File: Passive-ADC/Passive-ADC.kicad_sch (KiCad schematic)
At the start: 12 parts, among them J1 FPGA Terminal, J2 ADC Terminal

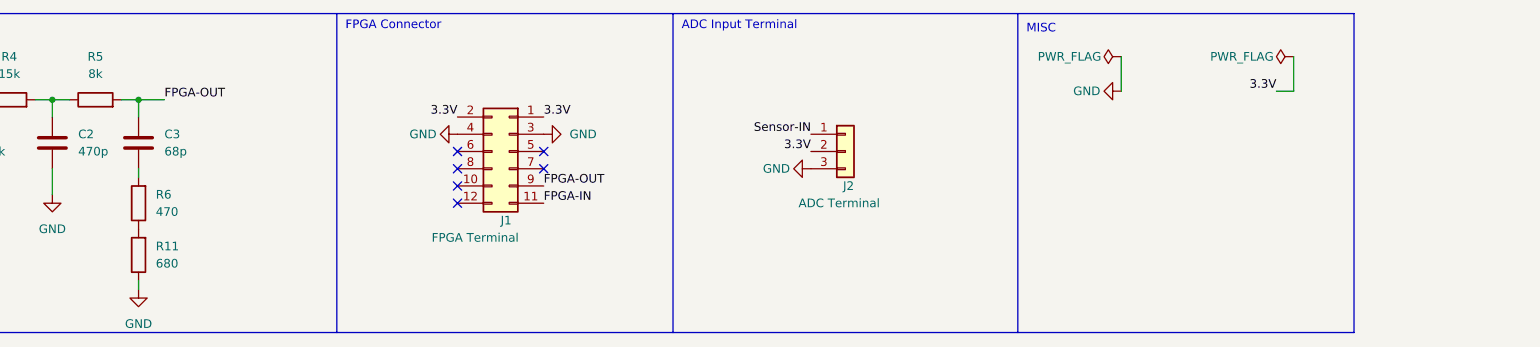
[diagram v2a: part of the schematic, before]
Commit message: Close to final pcb adjusted footprints and layout design incorperating voltage divider
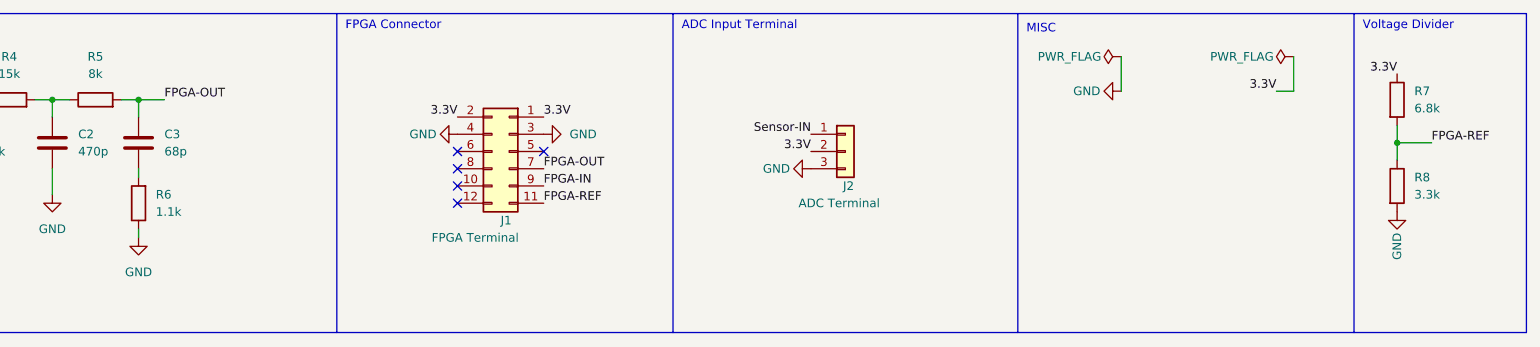
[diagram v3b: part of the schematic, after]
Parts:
- removed R11: 680, Resistor_SMD:R_0805_2012Metric_Pad1.20x1.40mm_HandSolder, symbol Device:R
- added R7: 6.8k, Resistor_SMD:R_0805_2012Metric_Pad1.20x1.40mm_HandSolder, symbol Device:R
- added R8: 3.3k, Resistor_SMD:R_0805_2012Metric_Pad1.20x1.40mm_HandSolder, symbol Device:R
- J1: footprint PinHeader_2x06_P1.00mm_Horizontal -> Connector_PinHeader_2.54mm:PinHeader_2x06_P2.54mm_Horizontal
- J2: footprint PinHeader_1x03_P1.00mm_Vertical -> Connector_PinHeader_2.54mm:PinHeader_1x03_P2.54mm_Vertical
- R6: value 470 -> 1.1k
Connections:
- net 3.3V: now also R7.1
- net FPGA-IN: now also J1.9 (Pin_9); no longer J1.11 (Pin_11)
- net FPGA-OUT: now also J1.7 (Pin_7); no longer J1.9 (Pin_9)
- net GND: now also R6.1, R8.2
- new net FPGA-REF: J1.11 (Pin_11), R7.2, R8.1
- no-connect marks 6 -> 5
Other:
- note added: "Voltage Divider"
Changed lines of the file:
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@@
   (junction (at 54.61 25.4) (diameter 0) (color 0 0 0 0)
   )
-  (no_connect (at 139.7 35.56))
+  (junction (at 265.43 31.75) (diameter 0) (color 0 0 0 0)
+  )
   (no_connect (at 127 33.02))
   (no_connect (at 127 35.56))
@@
     (stroke (width 0) (type default) (color 0 0 0 0))
   )
+  (wire (pts (xy 265.43 29.21) (xy 265.43 31.75))
+    (stroke (width 0) (type default) (color 0 0 0 0))
+  )
   (polyline (pts (xy 109.22 59.69) (xy 158.75 59.69))
     (stroke (width 0) (type default) (color 0 0 0 0))
@@
     (stroke (width 0) (type default) (color 0 0 0 0))
   )
+  (polyline (pts (xy 284.48 12.7) (xy 284.48 59.69))
+    (stroke (width 0) (type default) (color 0 0 0 0))
+  )
   (wire (pts (xy 80.01 35.56) (xy 80.01 36.83))
     (stroke (width 0) (type default) (color 0 0 0 0))
@@
     (stroke (width 0) (type default) (color 0 0 0 0))
   )
+  (polyline (pts (xy 284.48 59.69) (xy 259.08 59.69))
+    (stroke (width 0) (type default) (color 0 0 0 0))
+  )
   (wire (pts (xy 41.91 35.56) (xy 41.91 39.37))
     (stroke (width 0) (type default) (color 0 0 0 0))
   )
-  (wire (pts (xy 80.01 52.07) (xy 80.01 53.34))
+  (wire (pts (xy 80.01 44.45) (xy 80.01 45.72))
+    (stroke (width 0) (type default) (color 0 0 0 0))
+  )
+  (wire (pts (xy 265.43 31.75) (xy 270.51 31.75))
     (stroke (width 0) (type default) (color 0 0 0 0))
   )
@@
     (stroke (width 0) (type default) (color 0 0 0 0))
   )
+  (polyline (pts (xy 259.08 12.7) (xy 284.48 12.7))
+    (stroke (width 0) (type default) (color 0 0 0 0))
+  )
   (polyline (pts (xy 209.55 59.69) (xy 158.75 59.69))
     (stroke (width 0) (type default) (color 0 0 0 0))
@@
     (stroke (width 0) (type default) (color 0 0 0 0))
   )
+  (wire (pts (xy 265.43 31.75) (xy 265.43 34.29))
+    (stroke (width 0) (type default) (color 0 0 0 0))
+  )
   (wire (pts (xy 80.01 25.4) (xy 80.01 27.94))
     (stroke (width 0) (type default) (color 0 0 0 0))
@@
     (stroke (width 0) (type default) (color 0 0 0 0))
   )
+  (text "Voltage Divider\n" (at 260.35 15.24 0)
+    (effects (font (size 1.27 1.27)) (justify left bottom))
+  )
   (text "ADC Input Terminal" (at 160.02 15.24 0)
     (effects (font (size 1.27 1.27)) (justify left bottom))
@@
     (effects (font (size 1.27 1.27)) (justify left bottom))
   )
-  (label "FPGA-IN" (at 139.7 40.64 0)
+  (label "FPGA-IN" (at 139.7 38.1 0)
+    (effects (font (size 1.27 1.27)) (justify left bottom))
+  )
+  (label "FPGA-REF" (at 270.51 31.75 0)
+    (effects (font (size 1.27 1.27)) (justify left bottom))
+  )
+  (label "3.3V" (at 265.43 21.59 180)
+    (effects (font (size 1.27 1.27)) (justify right bottom))
+  )
+  (label "FPGA-REF" (at 139.7 40.64 0)
     (effects (font (size 1.27 1.27)) (justify left bottom))
   )
@@
     (effects (font (size 1.27 1.27)) (justify right bottom))
   )
-  (label "FPGA-OUT" (at 139.7 38.1 0)
+  (label "FPGA-OUT" (at 139.7 35.56 0)
     (effects (font (size 1.27 1.27)) (justify left bottom))
   )
@@
     (pin "2")
   )
+  (symbol (lib_id "power:GND") (at 265.43 41.91 0) (unit 1)
+    (in_bom yes) (on_board yes)
+    (property "Reference" "#PWR0101" (id 0) (at 265.43 48.26 0)
+      (effects (font (size 1.27 1.27)) hide)
+    )
+    (property "Value" "GND" (id 1) (at 265.43 46.99 90))
+    (property "Footprint" "" (id 2) (at 265.43 41.91 0)
+      (effects (font (size 1.27 1.27)) hide)
+    )
+    (property "Datasheet" "" (id 3) (at 265.43 41.91 0)
+      (effects (font (size 1.27 1.27)) hide)
+    )
+    (pin "1")
+  )
   (symbol (lib_id "power:GND") (at 127 30.48 270) (unit 1)
     (in_bom yes) (on_board yes)
@@
     (pin "1")
   )
-  (symbol (lib_id "power:GND") (at 80.01 53.34 0) (unit 1)
-    (in_bom yes) (on_board yes) (fields_autoplaced)
-    (property "Reference" "#PWR04" (id 0) (at 80.01 59.69 0)
-      (effects (font (size 1.27 1.27)) hide)
-    )
-    (property "Value" "GND" (id 1) (at 80.01 58.42 0))
-    (property "Footprint" "" (id 2) (at 80.01 53.34 0)
-      (effects (font (size 1.27 1.27)) hide)
-    )
-    (property "Datasheet" "" (id 3) (at 80.01 53.34 0)
-      (effects (font (size 1.27 1.27)) hide)
-    )
-    (pin "1")
-  )
-  (symbol (lib_id "Device:R") (at 80.01 48.26 180) (unit 1)
-    (in_bom yes) (on_board yes) (fields_autoplaced)
-    (property "Reference" "R11" (id 0) (at 82.55 46.9899 0)
-      (effects (font (size 1.27 1.27)) (justify right))
-    )
-    (property "Value" "680" (id 1) (at 82.55 49.5299 0)
-      (effects (font (size 1.27 1.27)) (justify right))
-    )
-    (property "Footprint" "Resistor_SMD:R_0805_2012Metric_Pad1.20x1.40mm_HandSolder" (id 2) (at 81.788 48.26 90)
-      (effects (font (size 1.27 1.27)) hide)
-    )
-    (property "Datasheet" "311-680CRTR-ND" (id 3) (at 80.01 48.26 0)
-      (effects (font (size 1.27 1.27)) hide)
-    )
-    (pin "1")
-    (pin "2")
+  (symbol (lib_id "power:GND") (at 80.01 45.72 0) (unit 1)
+    (in_bom yes) (on_board yes) (fields_autoplaced)
+    (property "Reference" "#PWR04" (id 0) (at 80.01 52.07 0)
+      (effects (font (size 1.27 1.27)) hide)
+    )
+    (property "Value" "GND" (id 1) (at 80.01 50.8 0))
+    (property "Footprint" "" (id 2) (at 80.01 45.72 0)
+      (effects (font (size 1.27 1.27)) hide)
+    )
+    (property "Datasheet" "" (id 3) (at 80.01 45.72 0)
+      (effects (font (size 1.27 1.27)) hide)
+    )
+    (pin "1")
   )
   (symbol (lib_id "power:GND") (at 179.07 35.56 270) (unit 1)
@@
       (effects (font (size 1.27 1.27)) (justify right))
     )
-    (property "Value" "470" (id 1) (at 82.55 41.9099 0)
+    (property "Value" "1.1k" (id 1) (at 82.55 41.9099 0)
       (effects (font (size 1.27 1.27)) (justify right))
     )
@@
       (effects (font (size 1.27 1.27)) (justify right))
     )
-    (property "Footprint" "PinHeader_1x03_P1.00mm_Vertical" (id 2) (at 184.15 33.02 0)
+    (property "Footprint" "Connector_PinHeader_2.54mm:PinHeader_1x03_P2.54mm_Vertical" (id 2) (at 184.15 33.02 0)
       (effects (font (size 1.27 1.27)) hide)
     )
@@
     (pin "2")
   )
+  (symbol (lib_id "Device:R") (at 265.43 38.1 0) (unit 1)
+    (in_bom yes) (on_board yes) (fields_autoplaced)
+    (property "Reference" "R8" (id 0) (at 267.97 36.8299 0)
+      (effects (font (size 1.27 1.27)) (justify left))
+    )
+    (property "Value" "3.3k" (id 1) (at 267.97 39.3699 0)
+      (effects (font (size 1.27 1.27)) (justify left))
+    )
+    (property "Footprint" "Resistor_SMD:R_0805_2012Metric_Pad1.20x1.40mm_HandSolder" (id 2) (at 263.652 38.1 90)
+      (effects (font (size 1.27 1.27)) hide)
+    )
+    (property "Datasheet" "~" (id 3) (at 265.43 38.1 0)
+      (effects (font (size 1.27 1.27)) hide)
+    )
+    (pin "1")
+    (pin "2")
+  )
   (symbol (lib_id "Device:C") (at 80.01 31.75 0) (unit 1)
     (in_bom yes) (on_board yes) (fields_autoplaced)
@@
     (pin "1")
   )
+  (symbol (lib_id "Device:R") (at 265.43 25.4 0) (unit 1)
+    (in_bom yes) (on_board yes) (fields_autoplaced)
+    (property "Reference" "R7" (id 0) (at 267.97 24.1299 0)
+      (effects (font (size 1.27 1.27)) (justify left))
+    )
+    (property "Value" "6.8k" (id 1) (at 267.97 26.6699 0)
+      (effects (font (size 1.27 1.27)) (justify left))
+    )
+    (property "Footprint" "Resistor_SMD:R_0805_2012Metric_Pad1.20x1.40mm_HandSolder" (id 2) (at 263.652 25.4 90)
+      (effects (font (size 1.27 1.27)) hide)
+    )
+    (property "Datasheet" "~" (id 3) (at 265.43 25.4 0)
+      (effects (font (size 1.27 1.27)) hide)
+    )
+    (pin "1")
+    (pin "2")
+  )
   (symbol (lib_id "Connector_Generic:Conn_02x06_Odd_Even") (at 134.62 33.02 0) (mirror y) (unit 1)
     (in_bom yes) (on_board yes)
@@
       (effects (font (size 1.27 1.27)) (justify right))
     )
-    (property "Footprint" "PinHeader_2x06_P1.00mm_Horizontal" (id 2) (at 134.62 33.02 0)
+    (property "Footprint" "Connector_PinHeader_2.54mm:PinHeader_2x06_P2.54mm_Horizontal" (id 2) (at 134.62 33.02 0)
       (effects (font (size 1.27 1.27)) hide)
     )
@@
       (reference "#PWR08") (unit 1) (value "GND") (footprint "")
     )
+    (path "/2714a355-fe77-428f-9f9e-c180ec5677bb"
+      (reference "#PWR0101") (unit 1) (value "GND") (footprint "")
+    )
     (path "/1e9f2ce0-6d08-46ba-8d06-09c985b358e9"
       (reference "C1") (unit 1) (value ".1u") (footprint "Capacitor_SMD:C_0805_2012Metric_Pad1.18x1.45mm_HandSolder")
@@
     )
     (path "/fbc3ac75-825f-438a-85e7-381ae2adaad7"
-      (reference "J1") (unit 1) (value "FPGA Terminal") (footprint "PinHeader_2x06_P1.00mm_Horizontal")
+      (reference "J1") (unit 1) (value "FPGA Terminal") (footprint "Connector_PinHeader_2.54mm:PinHeader_2x06_P2.54mm_Horizontal")
     )
     (path "/85b6ba71-4dfc-4729-8bf7-4aaca5952350"
-      (reference "J2") (unit 1) (value "ADC Terminal") (footprint "PinHeader_1x03_P1.00mm_Vertical")
+      (reference "J2") (unit 1) (value "ADC Terminal") (footprint "Connector_PinHeader_2.54mm:PinHeader_1x03_P2.54mm_Vertical")
     )
     (path "/da851561-7fdb-4f61-b0c2-2413cfd57a0f"
@@
     )
     (path "/84aecc63-06ed-478f-8f5f-d0d1edf5fbec"
-      (reference "R6") (unit 1) (value "470") (footprint "Resistor_SMD:R_0805_2012Metric_Pad1.20x1.40mm_HandSolder")
-    )
-    (path "/5e47f54a-9bfa-4e34-91af-e6176f5d2e90"
-      (reference "R11") (unit 1) (value "680") (footprint "Resistor_SMD:R_0805_2012Metric_Pad1.20x1.40mm_HandSolder")
-    )
-  )
+      (reference "R6") (unit 1) (value "1.1k") (footprint "Resistor_SMD:R_0805_2012Metric_Pad1.20x1.40mm_HandSolder")
+    )
+    (path "/ef0379e1-0f33-4bf0-a68b-15a43eba97fd"
+      (reference "R7") (unit 1) (value "6.8k") (footprint "Resistor_SMD:R_0805_2012Metric_Pad1.20x1.40mm_HandSolder")
+    )
+    (path "/dbca836e-ad49-43bf-a290-afd9b5a6b37a"
+      (reference "R8") (unit 1) (value "3.3k") (footprint "Resistor_SMD:R_0805_2012Metric_Pad1.20x1.40mm_HandSolder")
+    )
+  )

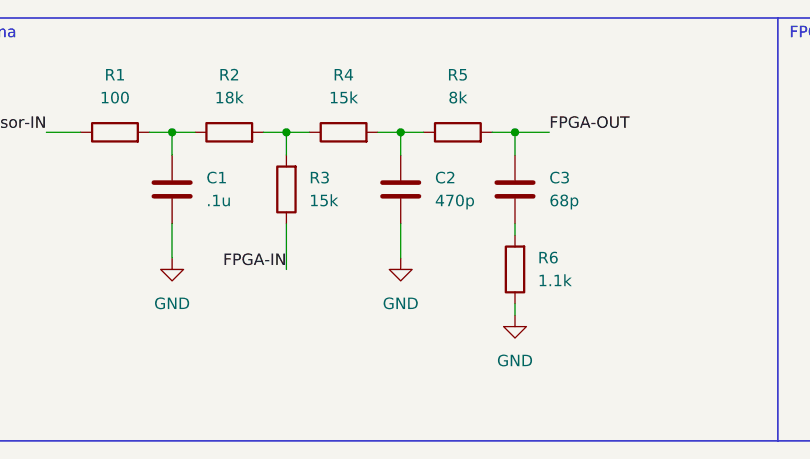
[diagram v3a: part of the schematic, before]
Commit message: Updated models with new schematic details
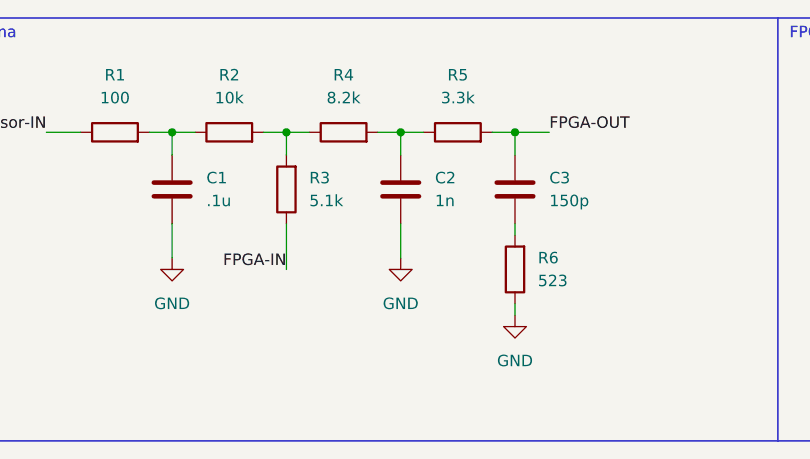
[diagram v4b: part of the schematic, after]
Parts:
- C2: value 470p -> 1n
- C3: value 68p -> 150p
- R2: value 18k -> 10k
- R3: value 15k -> 5.1k
- R4: value 15k -> 8.2k
- R5: value 8k -> 3.3k
- R6: value 1.1k -> 523
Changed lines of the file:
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@@
     (in_bom yes) (on_board yes) (fields_autoplaced)
     (property "Reference" "R5" (id 0) (at 73.66 19.05 90))
-    (property "Value" "8k" (id 1) (at 73.66 21.59 90))
+    (property "Value" "3.3k" (id 1) (at 73.66 21.59 90))
     (property "Footprint" "Resistor_SMD:R_0805_2012Metric_Pad1.20x1.40mm_HandSolder" (id 2) (at 73.66 27.178 90)
       (effects (font (size 1.27 1.27)) hide)
     )
-    (property "Datasheet" "Y1629-8.00KATR-ND" (id 3) (at 73.66 25.4 0)
+    (property "Datasheet" "311-3.3KARTR-ND" (id 3) (at 73.66 25.4 0)
       (effects (font (size 1.27 1.27)) hide)
     )
@@
     (in_bom yes) (on_board yes) (fields_autoplaced)
     (property "Reference" "R4" (id 0) (at 60.96 19.05 90))
-    (property "Value" "15k" (id 1) (at 60.96 21.59 90))
+    (property "Value" "8.2k" (id 1) (at 60.96 21.59 90))
     (property "Footprint" "Resistor_SMD:R_0805_2012Metric_Pad1.20x1.40mm_HandSolder" (id 2) (at 60.96 27.178 90)
       (effects (font (size 1.27 1.27)) hide)
     )
-    (property "Datasheet" "13-RC0805FR-1315KLTR-ND" (id 3) (at 60.96 25.4 0)
+    (property "Datasheet" "311-8.2KARTR-ND" (id 3) (at 60.96 25.4 0)
       (effects (font (size 1.27 1.27)) hide)
     )
@@
       (effects (font (size 1.27 1.27)) (justify right))
     )
-    (property "Value" "1.1k" (id 1) (at 82.55 41.9099 0)
+    (property "Value" "523" (id 1) (at 82.55 41.9099 0)
       (effects (font (size 1.27 1.27)) (justify right))
     )
@@
       (effects (font (size 1.27 1.27)) hide)
     )
-    (property "Datasheet" "311-470CRTR-ND" (id 3) (at 80.01 40.64 0)
+    (property "Datasheet" "311-523CRTR-ND" (id 3) (at 80.01 40.64 0)
       (effects (font (size 1.27 1.27)) hide)
     )
@@
       (effects (font (size 1.27 1.27)) (justify right))
     )
-    (property "Value" "15k" (id 1) (at 57.15 33.0199 0)
+    (property "Value" "5.1k" (id 1) (at 57.15 33.0199 0)
       (effects (font (size 1.27 1.27)) (justify right))
     )
@@
       (effects (font (size 1.27 1.27)) hide)
     )
-    (property "Datasheet" "13-RC0805FR-1315KLTR-ND" (id 3) (at 54.61 31.75 0)
+    (property "Datasheet" "311-5.1KARTR-ND" (id 3) (at 54.61 31.75 0)
       (effects (font (size 1.27 1.27)) hide)
     )
@@
     (in_bom yes) (on_board yes) (fields_autoplaced)
     (property "Reference" "R2" (id 0) (at 48.26 19.05 90))
-    (property "Value" "18k" (id 1) (at 48.26 21.59 90))
+    (property "Value" "10k" (id 1) (at 48.26 21.59 90))
     (property "Footprint" "Resistor_SMD:R_0805_2012Metric_Pad1.20x1.40mm_HandSolder" (id 2) (at 48.26 27.178 90)
       (effects (font (size 1.27 1.27)) hide)
     )
-    (property "Datasheet" "A129703TR-ND" (id 3) (at 48.26 25.4 0)
+    (property "Datasheet" "311-10KARTR-ND" (id 3) (at 48.26 25.4 0)
       (effects (font (size 1.27 1.27)) hide)
     )
@@
       (effects (font (size 1.27 1.27)) (justify left))
     )
-    (property "Value" "470p" (id 1) (at 71.12 33.0199 0)
+    (property "Value" "1n" (id 1) (at 71.12 33.0199 0)
       (effects (font (size 1.27 1.27)) (justify left))
     )
@@
       (effects (font (size 1.27 1.27)) hide)
     )
-    (property "Datasheet" "1276-2514-2-ND" (id 3) (at 67.31 31.75 0)
+    (property "Datasheet" "478-1371-2-ND" (id 3) (at 67.31 31.75 0)
       (effects (font (size 1.27 1.27)) hide)
     )
@@
       (effects (font (size 1.27 1.27)) hide)
     )
-    (property "Datasheet" "~" (id 3) (at 265.43 38.1 0)
+    (property "Datasheet" "311-3.3KARTR-ND" (id 3) (at 265.43 38.1 0)
       (effects (font (size 1.27 1.27)) hide)
     )
@@
       (effects (font (size 1.27 1.27)) (justify left))
     )
-    (property "Value" "68p" (id 1) (at 83.82 33.0199 0)
+    (property "Value" "150p" (id 1) (at 83.82 33.0199 0)
       (effects (font (size 1.27 1.27)) (justify left))
     )
@@
       (effects (font (size 1.27 1.27)) hide)
     )
-    (property "Datasheet" "1276-6680-2-ND" (id 3) (at 80.01 31.75 0)
+    (property "Datasheet" "478-1318-2-ND" (id 3) (at 80.01 31.75 0)
       (effects (font (size 1.27 1.27)) hide)
     )
@@
       (effects (font (size 1.27 1.27)) hide)
     )
-    (property "Datasheet" "~" (id 3) (at 265.43 25.4 0)
+    (property "Datasheet" "311-6.80KCRTR-ND" (id 3) (at 265.43 25.4 0)
       (effects (font (size 1.27 1.27)) hide)
     )
@@
     )
     (path "/c440b35e-3f7e-431c-90ab-fb12d5c34ace"
-      (reference "C2") (unit 1) (value "470p") (footprint "Capacitor_SMD:C_0805_2012Metric_Pad1.18x1.45mm_HandSolder")
+      (reference "C2") (unit 1) (value "1n") (footprint "Capacitor_SMD:C_0805_2012Metric_Pad1.18x1.45mm_HandSolder")
     )
     (path "/dd02a207-fa49-45c1-8a6d-f9dc54a91fee"
-      (reference "C3") (unit 1) (value "68p") (footprint "Capacitor_SMD:C_0805_2012Metric_Pad1.18x1.45mm_HandSolder")
+      (reference "C3") (unit 1) (value "150p") (footprint "Capacitor_SMD:C_0805_2012Metric_Pad1.18x1.45mm_HandSolder")
     )
     (path "/fbc3ac75-825f-438a-85e7-381ae2adaad7"
@@
     )
     (path "/a4a8430c-d7a1-47ce-bbb3-0b02aed0c1eb"
-      (reference "R2") (unit 1) (value "18k") (footprint "Resistor_SMD:R_0805_2012Metric_Pad1.20x1.40mm_HandSolder")
+      (reference "R2") (unit 1) (value "10k") (footprint "Resistor_SMD:R_0805_2012Metric_Pad1.20x1.40mm_HandSolder")
     )
     (path "/88afc6d6-80c2-449c-adb0-b4bcf7eec011"
-      (reference "R3") (unit 1) (value "15k") (footprint "Resistor_SMD:R_0805_2012Metric_Pad1.20x1.40mm_HandSolder")
+      (reference "R3") (unit 1) (value "5.1k") (footprint "Resistor_SMD:R_0805_2012Metric_Pad1.20x1.40mm_HandSolder")
     )
     (path "/699138f6-237a-4b8a-a4d4-7fb9091d901b"
-      (reference "R4") (unit 1) (value "15k") (footprint "Resistor_SMD:R_0805_2012Metric_Pad1.20x1.40mm_HandSolder")
+      (reference "R4") (unit 1) (value "8.2k") (footprint "Resistor_SMD:R_0805_2012Metric_Pad1.20x1.40mm_HandSolder")
     )
     (path "/0456c7de-9f79-46f5-a17e-4fa13a1b0cfc"
-      (reference "R5") (unit 1) (value "8k") (footprint "Resistor_SMD:R_0805_2012Metric_Pad1.20x1.40mm_HandSolder")
+      (reference "R5") (unit 1) (value "3.3k") (footprint "Resistor_SMD:R_0805_2012Metric_Pad1.20x1.40mm_HandSolder")
     )
     (path "/84aecc63-06ed-478f-8f5f-d0d1edf5fbec"
-      (reference "R6") (unit 1) (value "1.1k") (footprint "Resistor_SMD:R_0805_2012Metric_Pad1.20x1.40mm_HandSolder")
+      (reference "R6") (unit 1) (value "523") (footprint "Resistor_SMD:R_0805_2012Metric_Pad1.20x1.40mm_HandSolder")
     )
     (path "/ef0379e1-0f33-4bf0-a68b-15a43eba97fd"
